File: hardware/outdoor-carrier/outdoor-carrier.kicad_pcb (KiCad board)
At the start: 2 copper layers, 100 x 100 mm, 46 parts, among them J1 24 VAC, J2 Mode in 24 VAC, J3 XDB307 liquid, J4 XDB307 vapor, J5 XDB307 t.suction, J6 TH1 suction, J7 TH2 liquid, J8 SHT30 FS400, J9 TH3 t.suction, U1 ESP32 DevKit, U2 LM2596HV, U3 ADS1115 0x48, U4 ADS1115 0x49, U5 H11AA1, U6 H11AA1

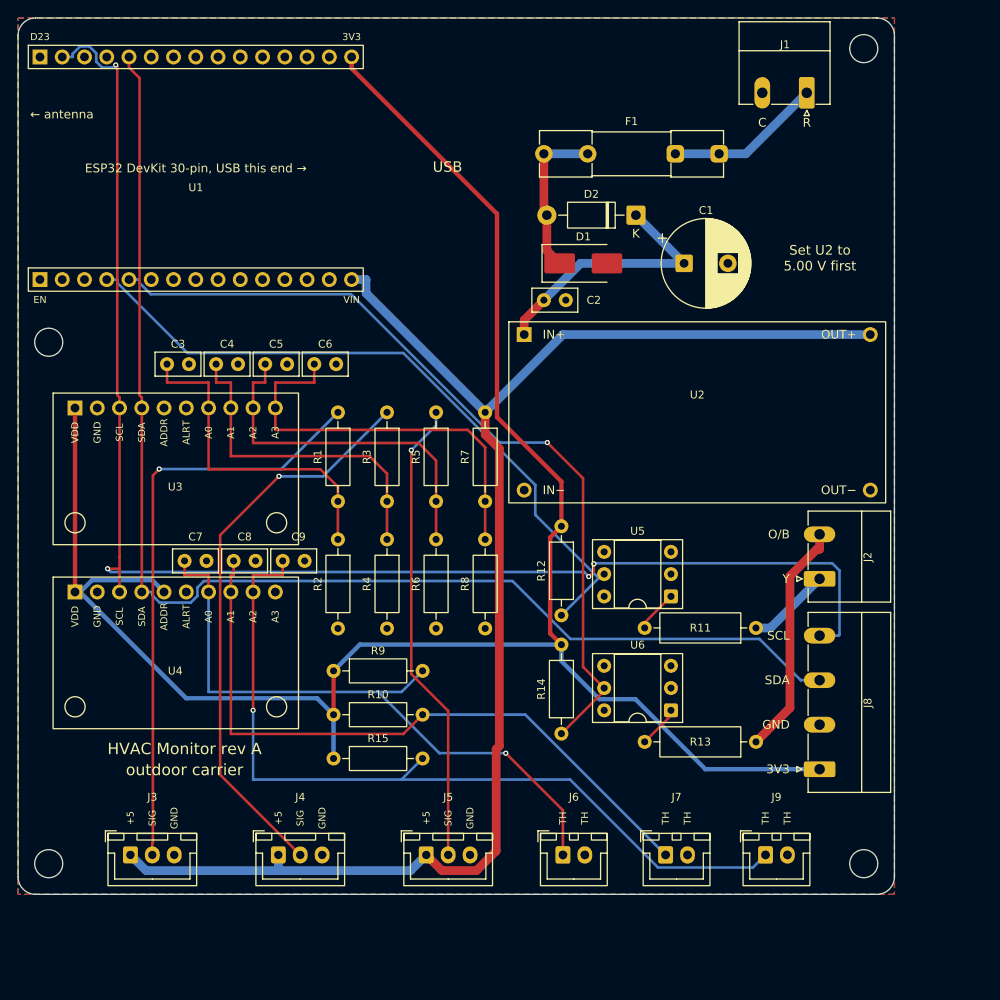
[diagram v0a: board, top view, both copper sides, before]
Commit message: Rev B layout: place, route and fab both carrier boards (DRC clean)
Boards: outdoor 110 x 110 mm, indoor 110 x 90 mm (both fit the Hammond 1554R2GY).
The top band is the same on both: the ESP32 (antenna keepout kept), the Wio-SX1262 at
the top edge with its u.FL toward the top wall, the AMS1117 and its caps, SW1 SETUP, and
the rev A power corner moved 10 mm right.
- Outdoor: CT jacks J11-J13 on the left edge. The footprint's own Edge.Cuts nose notch
  is part of the outline, using an edge-silk-trimmed copy in hvac_carrier. The CT
  passives (now 0805) and CT_BIAS sit beside the jacks. The ADS block is next to them,
  with the dividers and thermistor refs in 3.5 mm columns. The mode inputs are on the
  right, and J3-J10 are along the bottom.
- Indoor: TCA9548A, mux jacks J6-J10 along the bottom edge with their pull-ups,
  DS18B20 jacks on the left edge, and J5 on the right edge.
- preroute.py: the rev A hand routes no longer fit, so it is empty. route.py adds
  locked ground fan-out vias for SMD GND pads and a stitching via grid. It fixes
  starved GND thermals (45 degree spokes, then solid) and checks the result with
  kicad-cli. It also fixes a use-after-delete in the duplicate-track pass.
- route-all.sh retries Freerouting until DRC is clean. make_fab.py writes the
  gerbers zip, BOM, renders, schematic PDF, erc.rpt and drc.rpt.
DRC: 0 violations, 0 unconnected, 0 footprint errors (all severities, schematic
parity) on both boards. ERC: 0 errors, 0 warnings.

Co-Authored-By: Claude Opus 5.5 (1M context) <noreply@anthropic.com>
Claude-Session: https://claude.ai/code/session_01V4kWJ9CiBrt94u4WqUxFsk
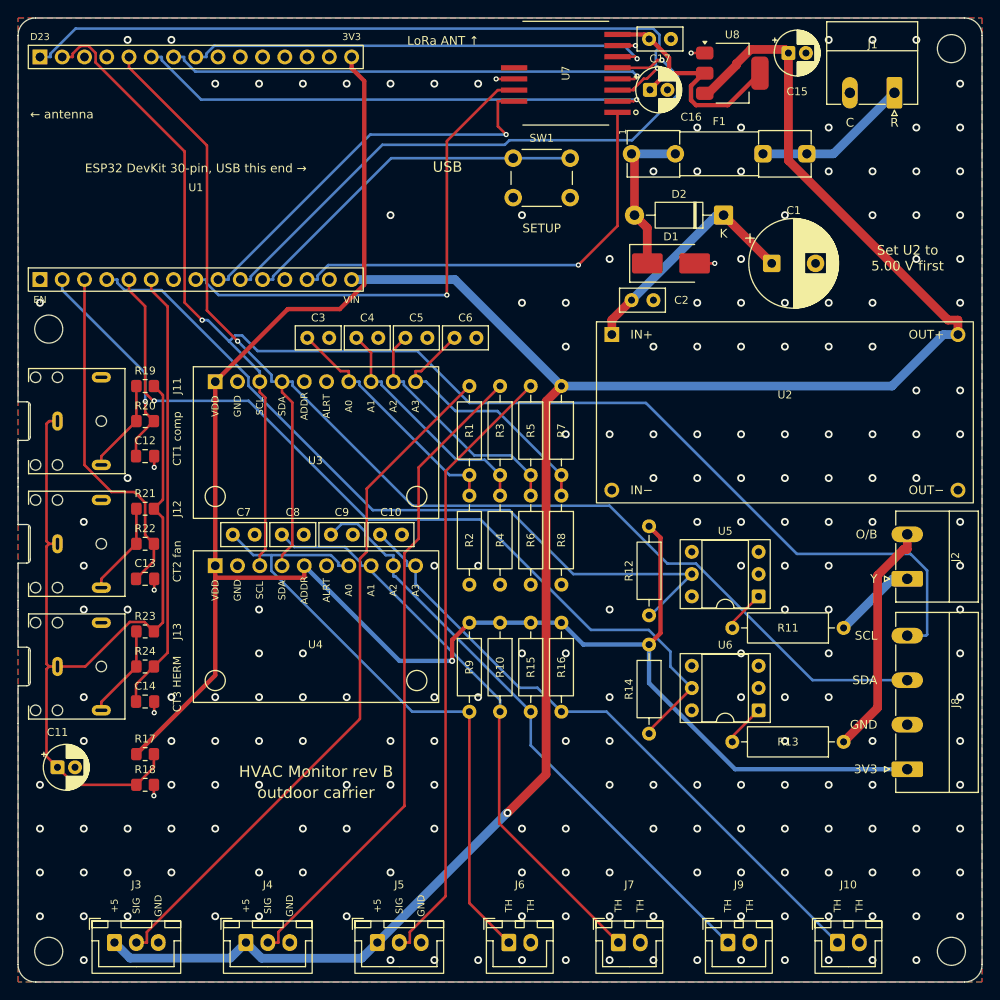
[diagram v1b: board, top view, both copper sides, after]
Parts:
- added C10: 0.1µF, Capacitor_THT:C_Disc_D5.0mm_W2.5mm_P2.50mm, F.Cu at (91.3, 109.0)
- added C11: 10µF 16V, Capacitor_THT:CP_Radial_D5.0mm_P2.00mm, F.Cu at (54.5, 135.5)
- added C12: 10nF, Capacitor_SMD:C_0805_2012Metric_Pad1.18x1.45mm_HandSolder, F.Cu at (64.5, 100.0)
- added C13: 10nF, Capacitor_SMD:C_0805_2012Metric_Pad1.18x1.45mm_HandSolder, F.Cu at (64.5, 114.0)
- added C14: 10nF, Capacitor_SMD:C_0805_2012Metric_Pad1.18x1.45mm_HandSolder, F.Cu at (64.5, 128.0)
- added C15: 10µF 16V, Capacitor_THT:CP_Radial_D5.0mm_P2.00mm, F.Cu at (137.9, 54.0)
- added C16: 22µF 10V, Capacitor_THT:CP_Radial_D5.0mm_P2.00mm, F.Cu at (122.1, 58.2)
- added C17: 0.1µF, Capacitor_THT:C_Disc_D5.0mm_W2.5mm_P2.50mm, F.Cu at (122.0, 52.4)
- added J10: TH4 discharge, Connector_JST:JST_XH_B2B-XH-A_1x02_P2.50mm_Vertical, F.Cu at (143.5, 155.5)
- added J11: CT1 compressor, hvac_carrier:Jack_3.5mm_CUI_SJ1-3523N_Horizontal_EdgeTrim, F.Cu at (54.5, 96.0)
- added J12: CT2 fan, hvac_carrier:Jack_3.5mm_CUI_SJ1-3523N_Horizontal_EdgeTrim, F.Cu at (54.5, 110.0)
- added J13: CT3 HERM, hvac_carrier:Jack_3.5mm_CUI_SJ1-3523N_Horizontal_EdgeTrim, F.Cu at (54.5, 124.0)
- added R16: 10k 0.1%, Resistor_THT:R_Axial_DIN0207_L6.3mm_D2.5mm_P10.16mm_Horizontal, F.Cu at (112.0, 119.0)
- added R17: 10k 1%, Resistor_SMD:R_0805_2012Metric_Pad1.20x1.40mm_HandSolder, F.Cu at (64.5, 134.0)
- added R18: 6.8k 1%, Resistor_SMD:R_0805_2012Metric_Pad1.20x1.40mm_HandSolder, F.Cu at (64.5, 137.5)
- added R19: 18 1%, Resistor_SMD:R_0805_2012Metric_Pad1.20x1.40mm_HandSolder, F.Cu at (64.5, 92.0)
- added R20: 1k, Resistor_SMD:R_0805_2012Metric_Pad1.20x1.40mm_HandSolder, F.Cu at (64.5, 96.0)
- added R21: DNP, Resistor_SMD:R_0805_2012Metric_Pad1.20x1.40mm_HandSolder, F.Cu at (64.5, 106.0)
- added R22: 1k, Resistor_SMD:R_0805_2012Metric_Pad1.20x1.40mm_HandSolder, F.Cu at (64.5, 110.0)
- added R23: DNP, Resistor_SMD:R_0805_2012Metric_Pad1.20x1.40mm_HandSolder, F.Cu at (64.5, 120.0)
- added R24: 1k, Resistor_SMD:R_0805_2012Metric_Pad1.20x1.40mm_HandSolder, F.Cu at (64.5, 124.0)
- added SW1: SETUP, Button_Switch_THT:SW_PUSH_6mm, F.Cu at (106.5, 66.0)
- added U7: Wio-SX1262, hvac_carrier:Wio_SX1262, F.Cu at (112.5, 56.3)
- added U8: AMS1117-3.3, Package_TO_SOT_SMD:SOT-223-3_TabPin2, F.Cu at (131.5, 56.3)
- R2, R4, R6: value 20k 1% -> 10k 1%
- R8: value 15k 1% -> 10k 1%
- moved R15 27.3 mm to (108.5, 119.0), turned to -90 degrees
- moved R10 21.7 mm to (105.0, 119.0), turned to -90 degrees
- moved R9 16.4 mm to (101.5, 119.0), turned to -90 degrees
- moved C3 16.3 mm to (83.0, 86.5)
- moved C4 16.3 mm to (88.6, 86.5)
- moved C5 16.3 mm to (94.2, 86.5)
- moved C6 16.3 mm to (99.8, 86.5)
- moved U3 16.3 mm to (72.5, 91.5)
- moved U4 16.3 mm to (72.5, 112.5)
- moved R2 15.8 mm to (101.5, 104.5)
- moved R1 15.3 mm to (101.5, 92.0)
- moved H3 14.1 mm to (156.5, 156.5)
- moved R4 13.8 mm to (105.0, 104.5)
- moved R3 13.2 mm to (105.0, 92.0)
- moved R6 11.9 mm to (108.5, 104.5)
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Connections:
- U1 pad 10: unconnected-(U1-D27-Pad10) -> /LORA_NRST
- U1 pad 11: unconnected-(U1-D14-Pad11) -> /SETUP
- U1 pad 13: unconnected-(U1-D13-Pad13) -> /LORA_RFSW
- U1 pad 16: unconnected-(U1-D23-Pad16) -> /LORA_MOSI
- U1 pad 2: unconnected-(U1-VP-Pad2) -> /CT1_ADC
- U1 pad 21: unconnected-(U1-D19-Pad21) -> /LORA_MISO
- U1 pad 22: unconnected-(U1-D18-Pad22) -> /LORA_SCK
- U1 pad 23: unconnected-(U1-D5-Pad23) -> /LORA_NSS
- U1 pad 3: unconnected-(U1-VN-Pad3) -> /CT2_ADC
- U1 pad 6: unconnected-(U1-D32-Pad6) -> /CT3_ADC
- U1 pad 8: unconnected-(U1-D25-Pad8) -> /LORA_BUSY
- U1 pad 9: unconnected-(U1-D26-Pad9) -> /LORA_DIO1
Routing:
- net /CT_BIAS: track 0.00 -> 100.9 mm
- net /LORA_MOSI: track 0.00 -> 82.3 mm, vias 0 -> 1
- net /T_DIS: track 0.00 -> 73.0 mm
- net /LORA_NRST: track 0.00 -> 69.0 mm, vias 0 -> 1
- net +5V: track 167.6 -> 234.5 mm, vias 0 -> 1
- net /LORA_MISO: track 0.00 -> 59.9 mm, vias 0 -> 1
- net /LORA_BUSY: track 0.00 -> 57.3 mm, vias 0 -> 1
- net /LORA_SCK: track 0.00 -> 56.4 mm, vias 0 -> 1
- net /LORA_NSS: track 0.00 -> 54.1 mm, vias 0 -> 1
- net /LORA_RFSW: track 0.00 -> 51.2 mm, vias 0 -> 1
- net /CT3_ADC: track 0.00 -> 50.4 mm
- net /LORA_DIO1: track 0.00 -> 46.0 mm, vias 0 -> 1
- net /SETUP: track 0.00 -> 41.1 mm
- net /CT2_ADC: track 0.00 -> 39.8 mm
- net /+3V3_RF: track 0.00 -> 29.2 mm
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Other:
- board size 100 x 100 mm -> 110 x 110 mm
- board text added: "CT1 comp"
- board text added: "CT2 fan"
- board text added: "CT3 HERM"
- board text added: "HVAC Monitor rev B"
- board text added: "LoRa ANT ↑"
- board text added: "SETUP"
- board text removed: "HVAC Monitor rev A"

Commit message: Shrink rev B boards with the same parts: outdoor 100 x 100, indoor 100 x 88
The power corner is back at its rev A position. The radio's regulator, input cap and the
SETUP button moved right of C1, so the top band fits in 100 mm.
- Outdoor: the empty band is gone. The dividers sit under U2 in 3.5 mm columns, and the
  thermistor reference resistors sit under U4. Within JLCPCB's cheapest 100 x 100 size again.
- Indoor: J5 sits under U2 on the right edge and H3 is inside the board. The mux chip
  and pull-ups are under U2, and the U6 and 1-Wire pull-ups sit below the optos.
Both boards: DRC 0 violations, 0 unconnected, 0 footprint errors; ERC 0 / 0.
Box, plate and docs updated for the new sizes and holes; SETUP plunger moved with SW1.

Co-Authored-By: Claude Opus 5.5 (1M context) <noreply@anthropic.com>
Claude-Session: https://claude.ai/code/session_01V4kWJ9CiBrt94u4WqUxFsk
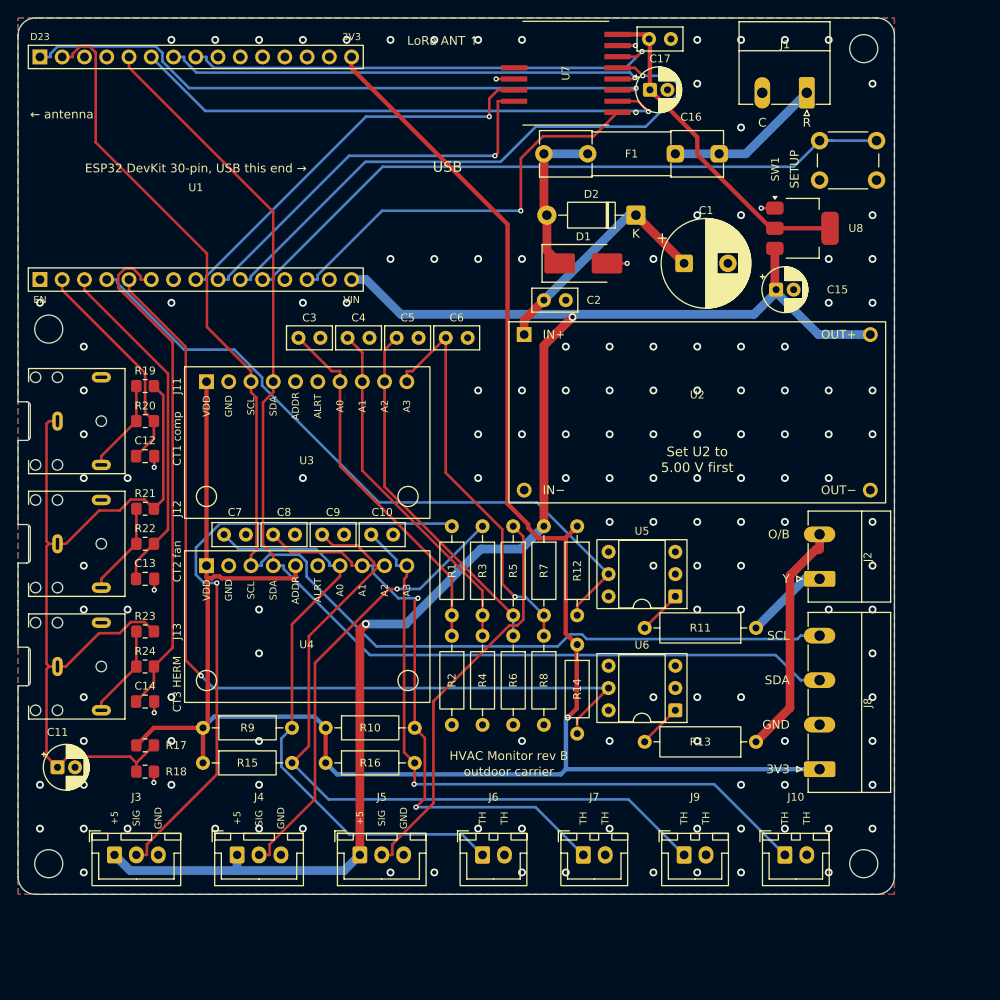
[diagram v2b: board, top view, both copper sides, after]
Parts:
- moved R15 40.7 mm to (71.1, 135.0), turned to 0 degrees
- moved SW1 35.0 mm to (141.5, 64.0)
- moved R9 32.7 mm to (71.1, 131.0), turned to 0 degrees
- moved R16 31.3 mm to (85.1, 135.0), turned to 0 degrees
- moved C15 27.0 mm to (136.5, 81.0)
- moved R10 23.2 mm to (85.1, 131.0), turned to 0 degrees
- moved U8 19.4 mm to (139.5, 74.0)
- moved R1 16.1 mm to (99.5, 108.0)
- moved R2 16.1 mm to (99.5, 120.5)
- moved R3 16.1 mm to (103.0, 108.0)
- moved R4 16.1 mm to (103.0, 120.5)
- moved R5 16.1 mm to (106.5, 108.0)
- moved R6 16.1 mm to (106.5, 120.5)
- moved R7 16.1 mm to (110.0, 108.0)
- moved R8 16.1 mm to (110.0, 120.5)
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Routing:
- net +5V: track 234.5 -> 177.3 mm, vias 1 -> 2
- net /SETUP: track 41.1 -> 78.3 mm
- net +3V3: track 206.5 -> 236.2 mm
- net /SCL: track 172.8 -> 143.2 mm, vias 1 -> 0
- net /P_TSUC_IN: track 70.4 -> 45.9 mm
- net /P_VAP_IN: track 75.2 -> 50.8 mm, vias 0 -> 1
- net /SDA: track 152.7 -> 133.8 mm, vias 1 -> 0
- net /V5_MON: track 30.6 -> 46.5 mm, vias 0 -> 1
- net /T_TSUC: track 69.4 -> 84.5 mm
- net /P_LIQ: track 28.3 -> 41.8 mm
- net /P_VAP: track 27.4 -> 40.4 mm
- net /P_TSUC: track 28.2 -> 40.7 mm
- net /LORA_BUSY: track 57.3 -> 46.7 mm
- net /MODE_Y: track 88.3 -> 78.1 mm
- net /LORA_MOSI: track 82.3 -> 73.5 mm
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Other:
- board size 110 x 110 mm -> 100 x 100 mm
